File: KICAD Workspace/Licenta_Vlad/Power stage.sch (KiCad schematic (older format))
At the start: 18 parts, among them J1 36V Battery, U5 LM2574HVM-12, U6 L7805, U7 LM2574HVM-12, U8 LP2950-3.3_TO92

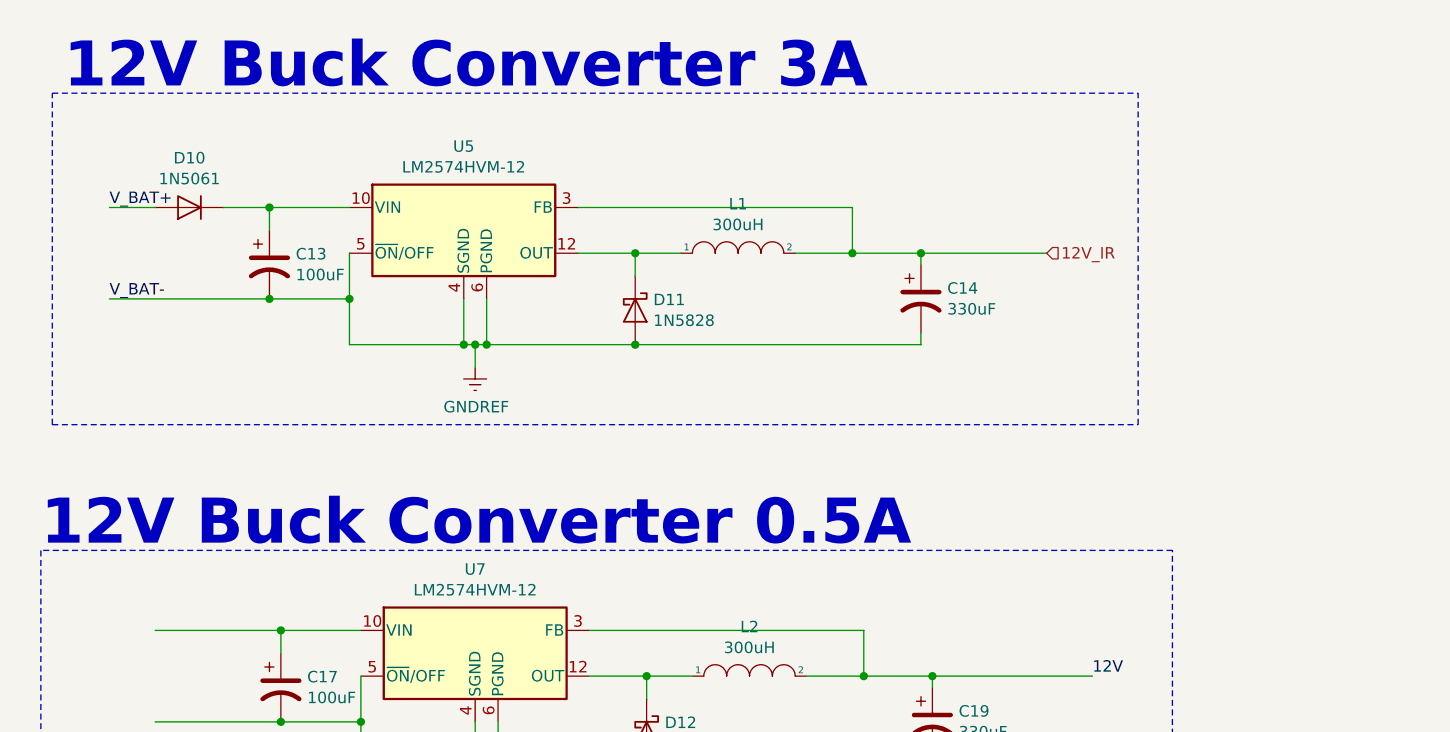
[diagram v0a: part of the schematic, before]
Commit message: SMD version
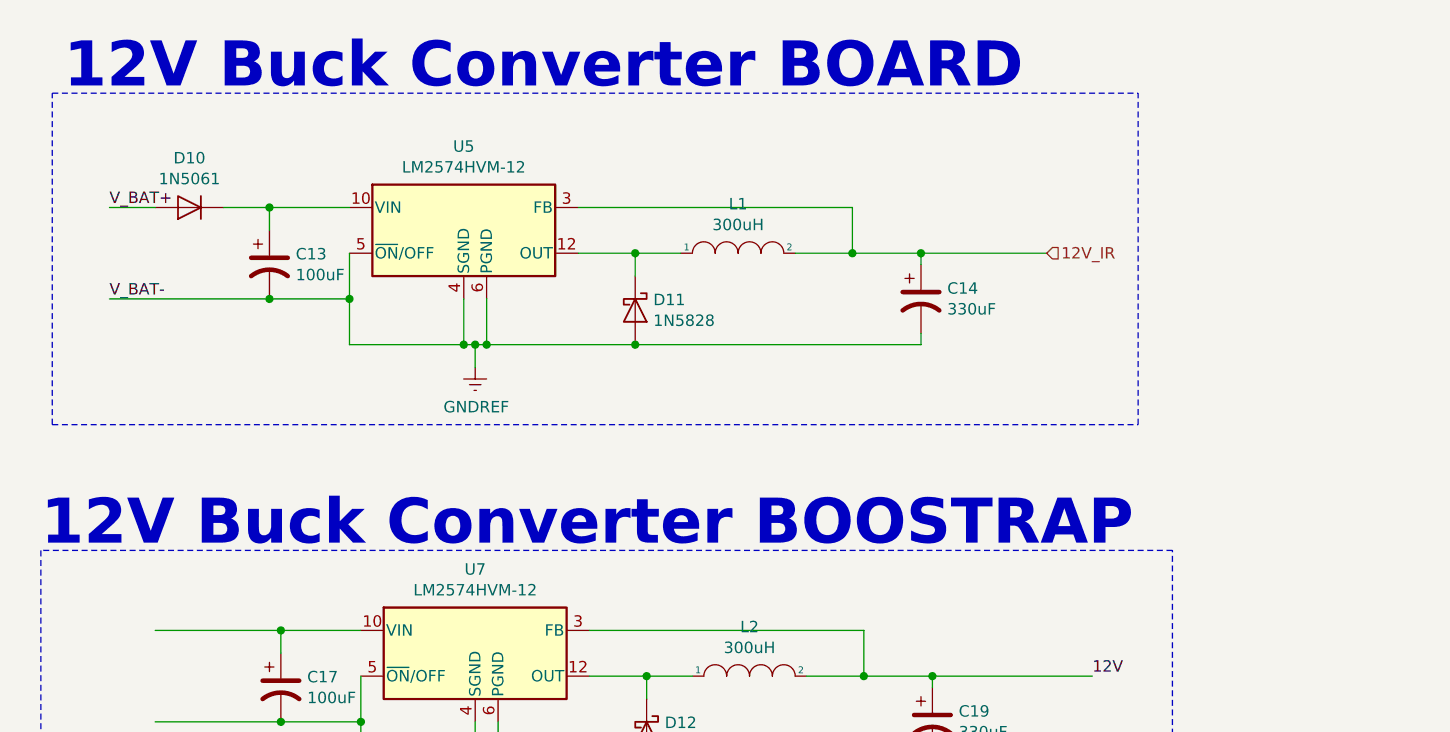
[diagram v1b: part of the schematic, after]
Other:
- note added: "12V Buck Converter BOARD"
- note added: "12V Buck Converter BOOSTRAP\n"
- note removed: "12V Buck Converter 0.5A"
- note removed: "12V Buck Converter 3A"
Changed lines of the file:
@@
 EESchema Schematic File Version 4
+LIBS:Power stage-cache
 EELAYER 26 0
 EELAYER END
 $Descr A4 11693 8268
 encoding utf-8
-Sheet 4 5
+Sheet 1 1
 Title ""
 Date ""
@@
 	1000 1250 5750 1250
 Text Notes 1050 1250 0    197  ~ 39
-12V Buck Converter 3A
+12V Buck Converter BOARD
 Wire Notes Line
 	1000 2700 5750 2700
@@
 	1450 3600 2000 3600
 Text Notes 950  3250 0    197  ~ 39
-12V Buck Converter 0.5A
+12V Buck Converter BOOSTRAP\n
 $Comp
 L Regulator_Linear:LP2950-3.3_TO92 U8
